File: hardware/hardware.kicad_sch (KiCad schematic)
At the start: 149 parts, among them J1 Conn_01x04_Pin, J10 Conn_01x03, J11 AVR-ISP-6, J12 Conn_01x03, J13 Conn_01x03, J14 Conn_01x03, J15 Conn_02x05_Odd_Even, J16 Conn_01x02, J2 Conn_01x04_Pin, J3 Conn_01x04_Pin, J4 Conn_01x04_Pin, J5 Conn_01x04_Pin, J6 Conn_01x04_Pin, J7 Conn_01x04_Pin, J8 Conn_01x03, J9 Conn_01x02, K1 G5Q-1, K3 G5Q-1, P1 USB_C_Plug, Q1 AO3400A, Q2 AO3400A, U1 DRV8825PWPR, U10 TPS562200, U11 LM317_SOT-223, U2 DRV8825PWPR, U3 DRV8825PWPR, U4 DRV8825PWPR, U5 DRV8825PWPR, U6 DRV8825PWPR, U7 DRV8825PWPR, U8 ATmega2560-16A, U9 CH340C, Y1 Crystal_GND24

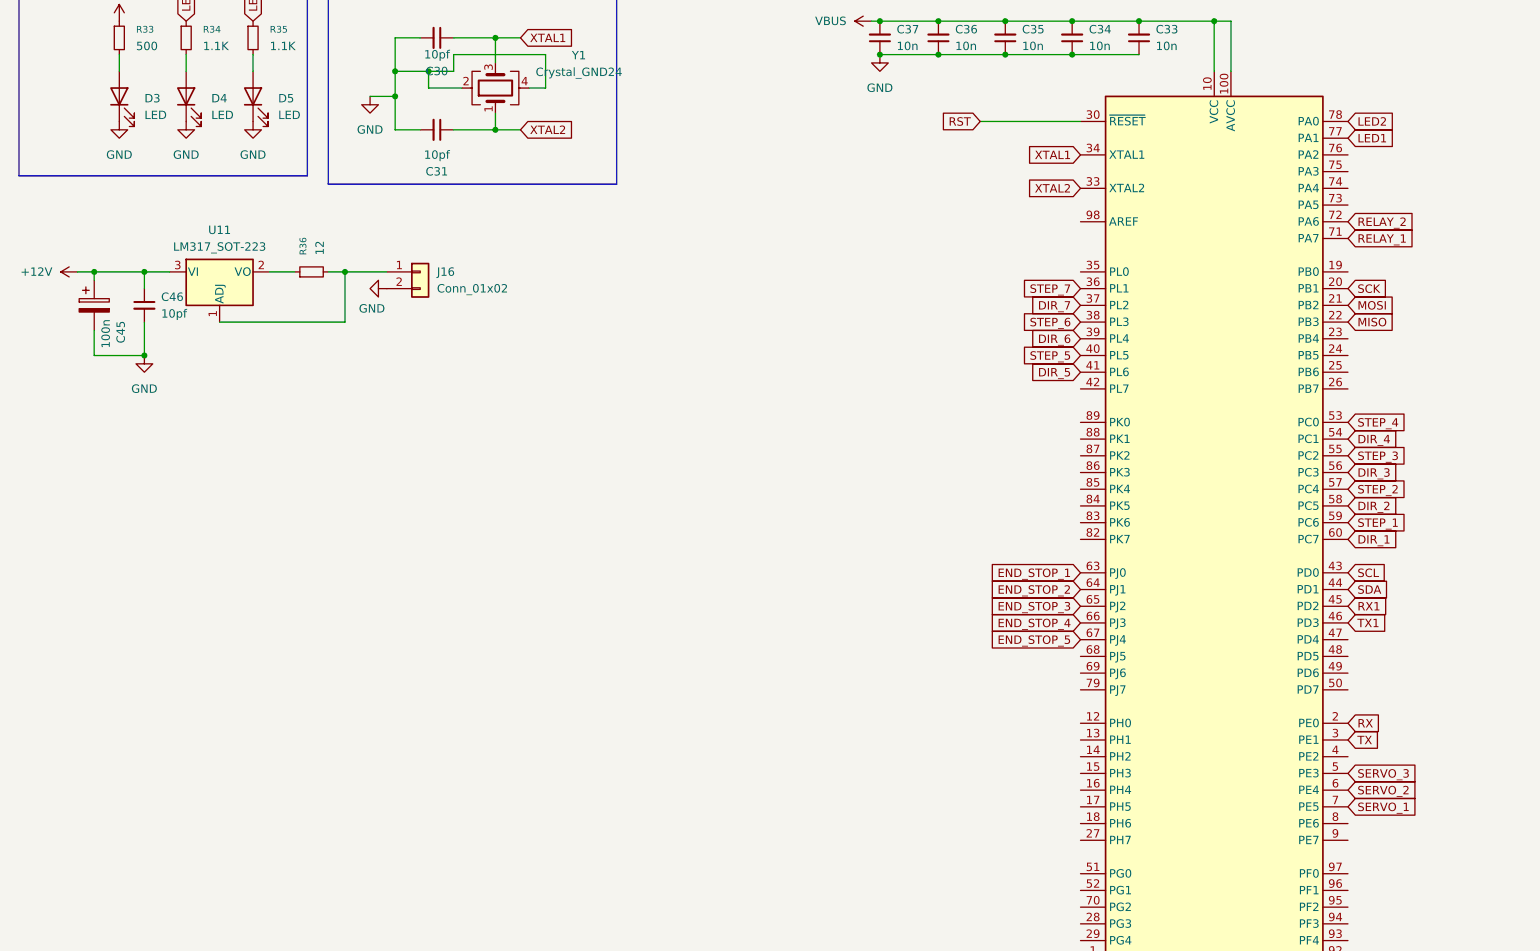
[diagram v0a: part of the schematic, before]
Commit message: add ftdi + buzzer + rst button
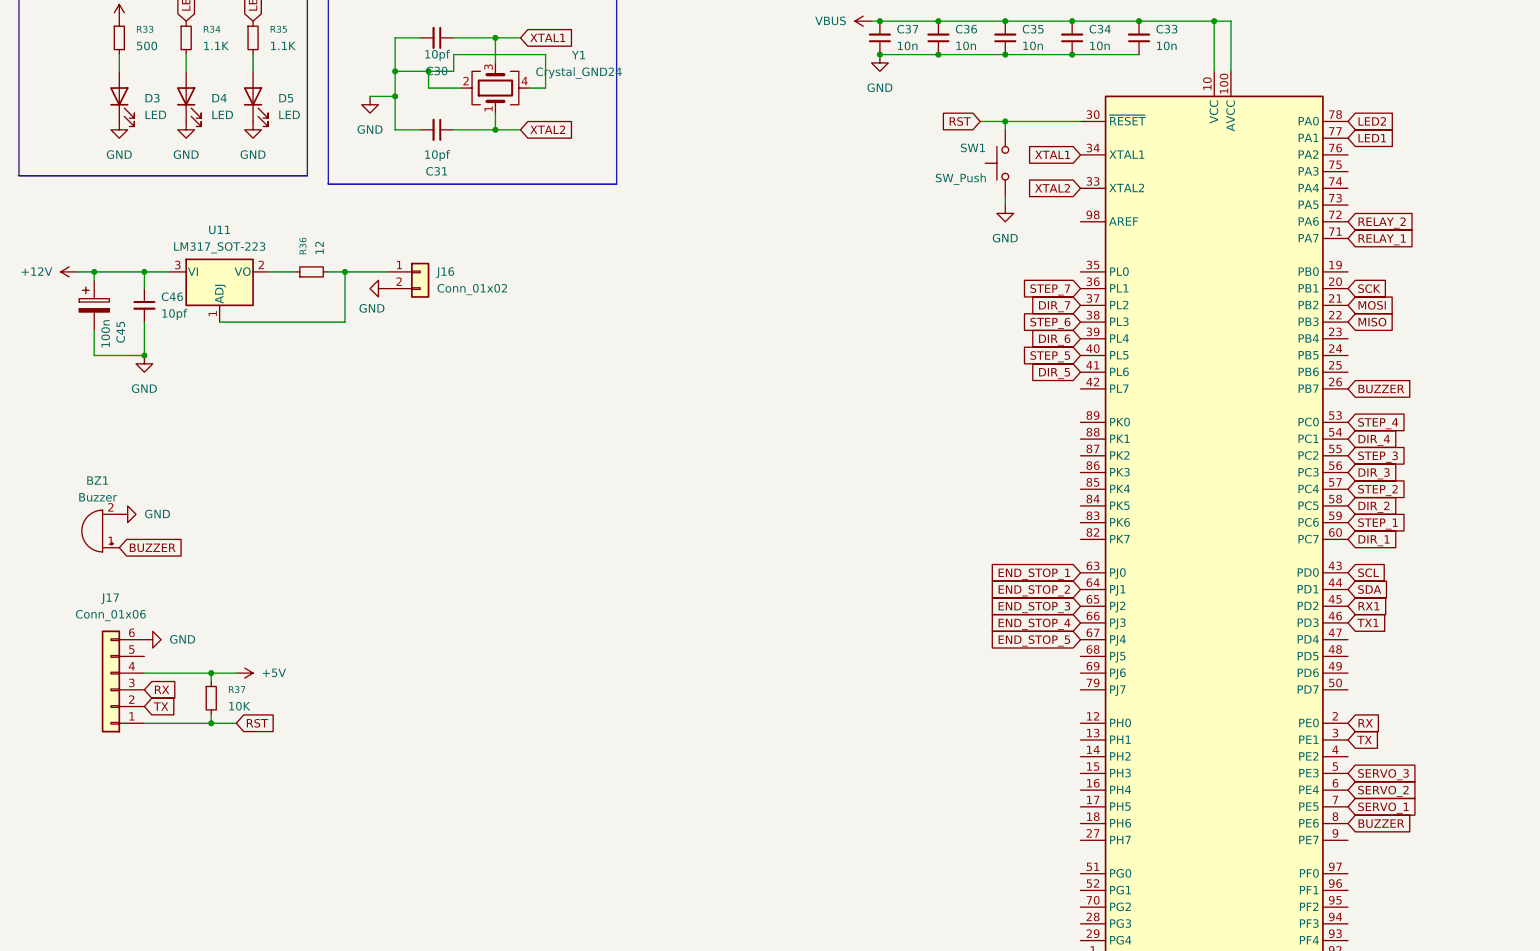
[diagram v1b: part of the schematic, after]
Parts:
- added BZ1: Buzzer, Buzzer_Beeper:Buzzer_TDK_PS1240P02BT_D12.2mm_H6.5mm, symbol Device:Buzzer
- added J17: Conn_01x06, Connector_PinHeader_2.54mm:PinHeader_1x06_P2.54mm_Vertical, symbol Connector_Generic:Conn_01x06
- added R37: 10K, Resistor_SMD:R_0603_1608Metric, symbol Device:R_Small
- added SW1: SW_Push, Button_Switch_SMD:SW_SPST_CK_RS282G05A3, symbol Switch:SW_Push
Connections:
- net +5V: now also J17.4 (Pin_4), R37.1
- net GND: now also BZ1.2 (-), J17.6 (Pin_6), SW1.1
- net RST: now also J17.1 (Pin_1), R37.2, SW1.2
- net RX: now also J17.3 (Pin_3)
- net TX: now also J17.2 (Pin_2)
- net BUZZER: now reaches U8.26 (PB7)
- net BUZZER: now also U8.8 (PE6), BZ1.1 (+)
